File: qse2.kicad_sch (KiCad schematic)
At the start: 81 parts, among them J1 5-1814832-1, J2 5-1814832-1, J3 Conn_02x08_Odd_Even, J4 SJ-3524-SMT, J6 Conn_01x02, J7 B4B-XH-A_LF__SN_, U1 SN74LVC1G14DBV, U10 SN74LVC1G14DBV, U11 NCP114ASN330T1G, U2 SN74LVC1G14DBV, U3 SN74CBT3253, U4 SN74AC74PW, U5 AD8137ARZ-R7, U6 NCV8114ASN165T1G, U7 UA78M05IDCYR, U8 AP2120N-2.5TRG1, U9 AD8137ARZ-R7

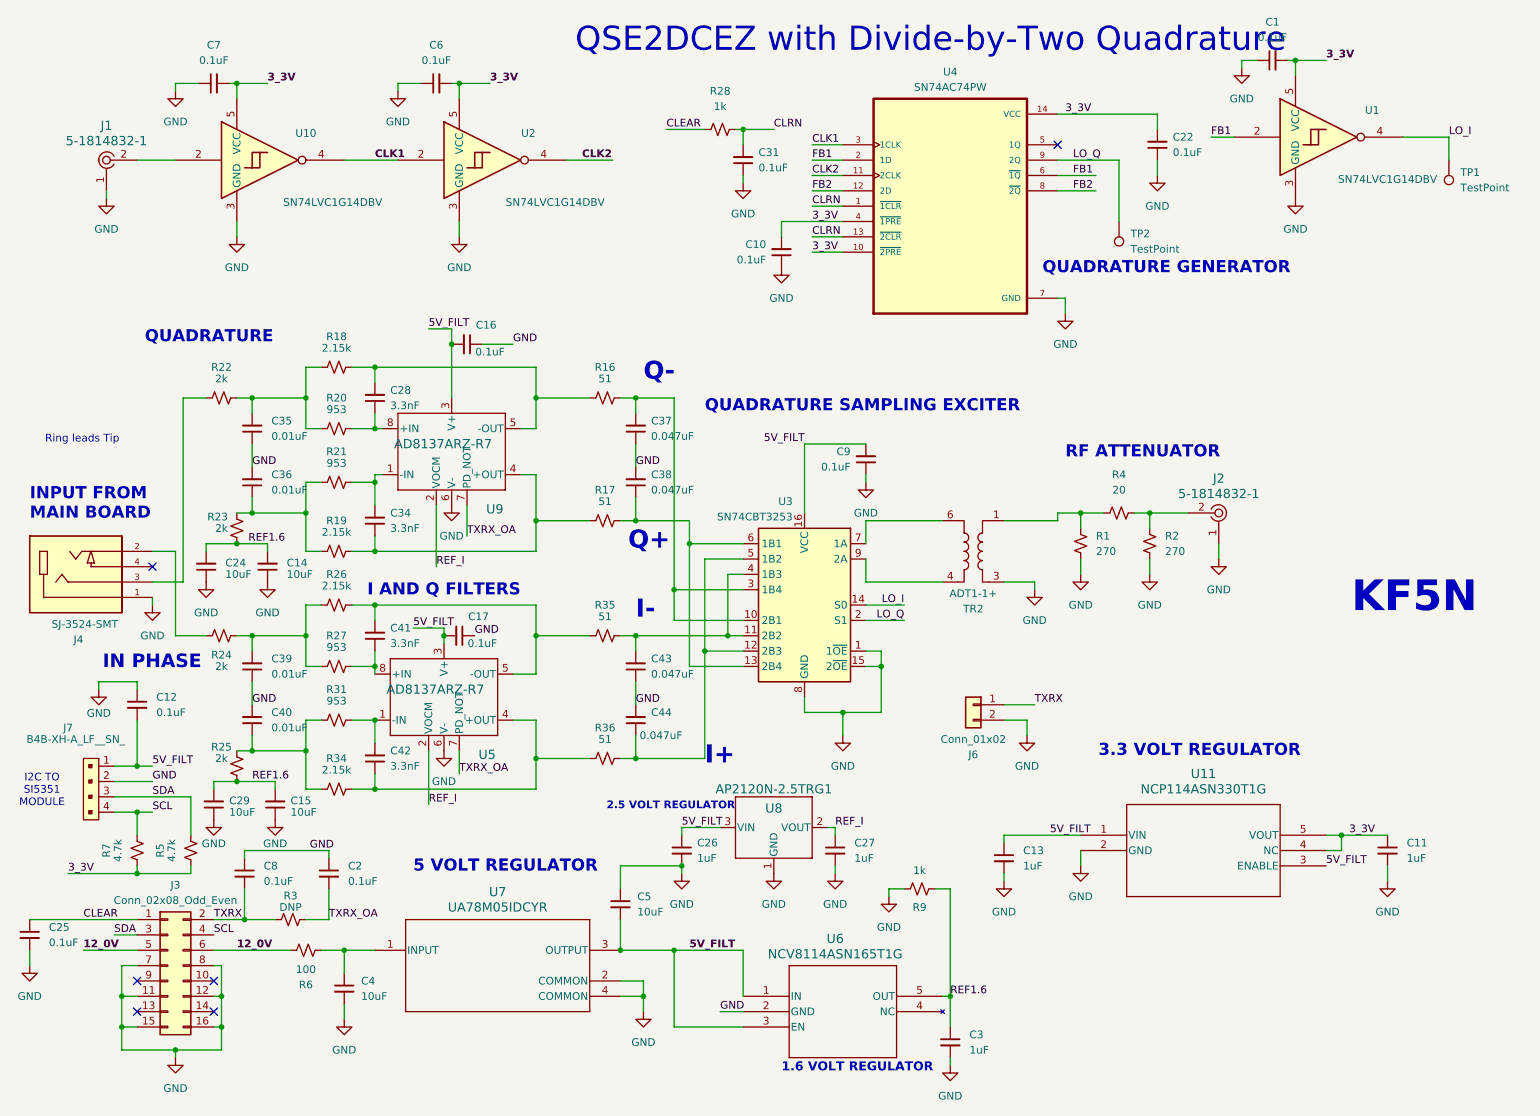
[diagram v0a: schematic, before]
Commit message: Work in progress. Changing reference sources due to supply chain issue.
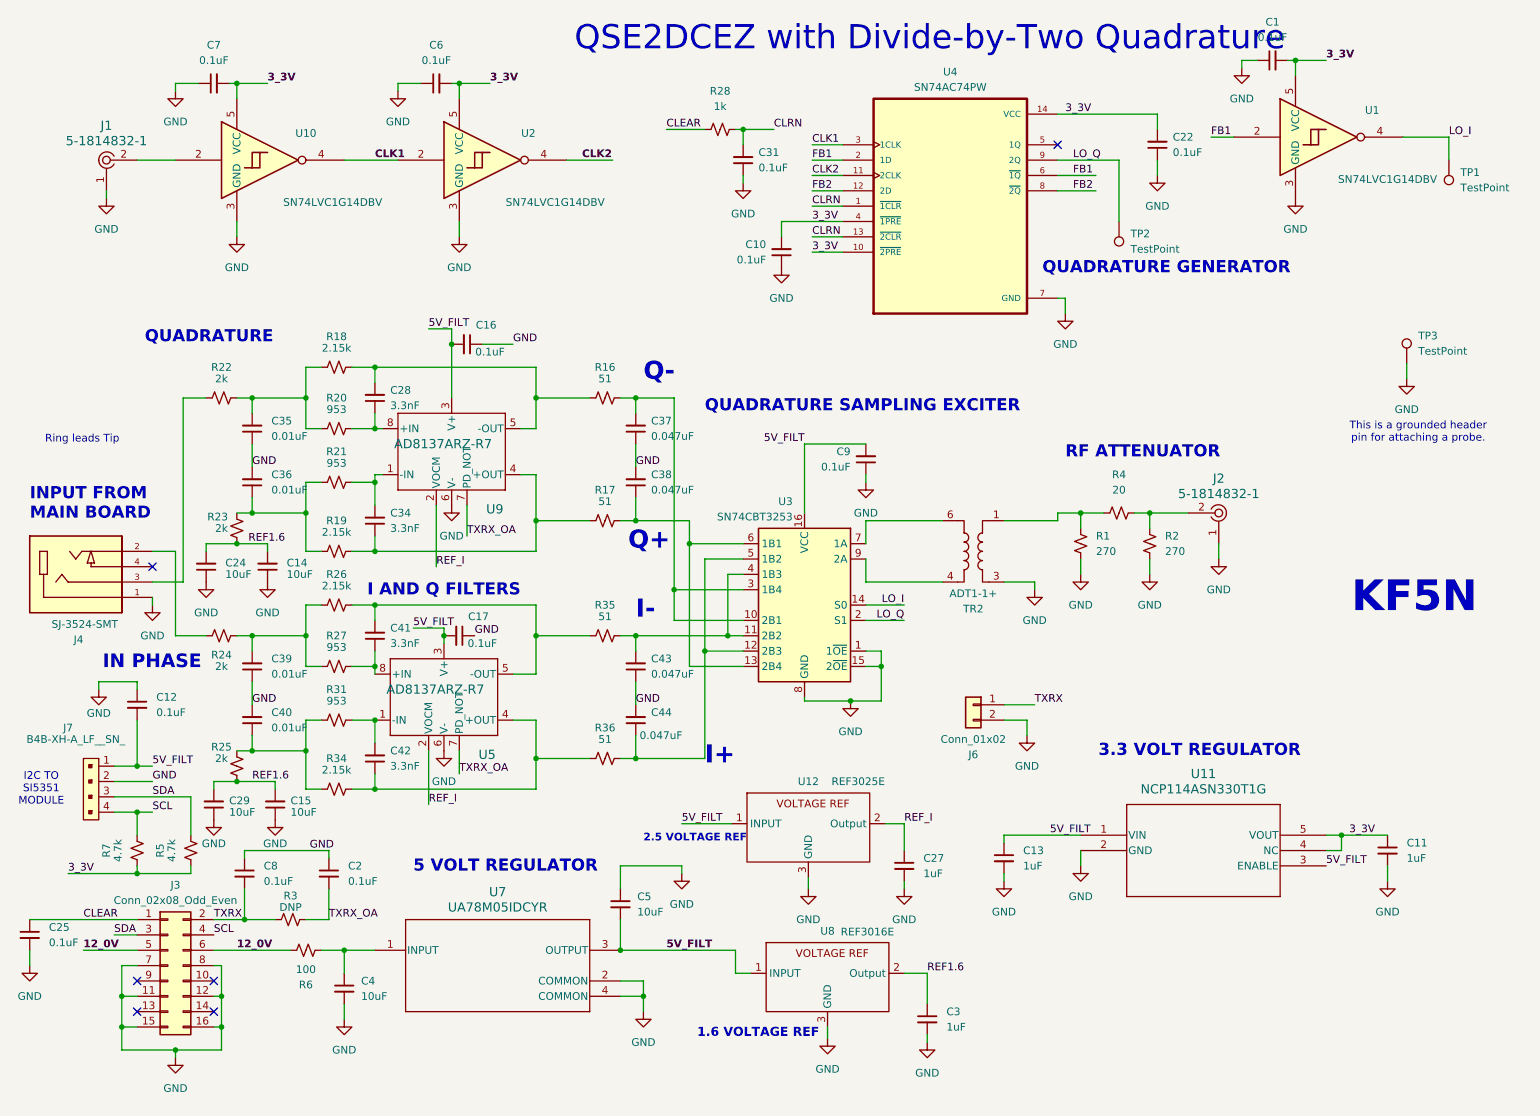
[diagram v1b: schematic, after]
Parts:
- removed C26: 1uF, Capacitor_SMD:C_1206_3216Metric, symbol Device:C_Small
- removed R9: 1k, Resistor_SMD:R_1206_3216Metric, symbol Device:R_Small_US
- removed U6: NCV8114ASN165T1G, TSOP-5-483-N_ONS, symbol NCP115ASN330T2G:NCP115ASN330T2G
- removed U8: AP2120N-2.5TRG1, AP2120N:SOT-23_DIO, symbol 2023-10-04_14-49-55:AP2120N-2.5TRG1
- added TP3: TestPoint, Connector_PinHeader_2.54mm:PinHeader_1x01_P2.54mm_Vertical, symbol Connector:TestPoint
- added U12: REF3025E, Package_TO_SOT_SMD:SOT-23-3, symbol TI_SOT23_vref:TI_SOT-23_vref
- added U8: REF3016E, Package_TO_SOT_SMD:SOT-23-3, symbol TI_SOT23_vref:TI_SOT-23_vref
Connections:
- net 5V_FILT: now also U12.1 (INPUT), U8.1 (INPUT)
- net GND: now also TP3.1, U12.3 (GND), U8.3 (GND)
- net REF1.6: now also U8.2 (Output)
- net REF_I: now also U12.2 (Output)
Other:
- note added: "1.6 VOLTAGE REF"
- note added: "2.5 VOLTAGE REF"
- note added: "This is a grounded header pin for attaching a probe."
- note removed: "1.6 VOLT REGULATOR"
- note removed: "2.5 VOLT REGULATOR"
- moved on the sheet: C27, C3

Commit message: Ready for release to fab.
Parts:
- removed C2: 0.1uF, Capacitor_SMD:C_1206_3216Metric, symbol Device:C_Small
- removed R3: DNP, Resistor_SMD:R_1206_3216Metric, symbol Device:R_Small_US
- removed U12: REF3025E, Package_TO_SOT_SMD:SOT-23-3, symbol TI_SOT23_vref:TI_SOT-23_vref
- added C18: 0.01uF, Capacitor_SMD:C_1206_3216Metric, symbol Device:C_Small
- added C30, C32: 1uF, Capacitor_SMD:C_1206_3216Metric, symbol Device:C_Small
- added R37: 2.2k, Resistor_SMD:R_1206_3216Metric, symbol Device:R_Small_US
- added U6: AP7343, Package_TO_SOT_SMD:TSOT-23-5, symbol AP7343-25W5-7:AP7343
- C27: value 1uF -> 10uF
- C8: value 0.1uF -> 0.01uF
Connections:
- net 5V_FILT: now also C30.1, C32.1, U6.1 (VIN), U6.3 (EN)
- net GND: now also C18.1, C30.2, C32.2, R37.1, U6.2 (GND)
- net REF_I: now also R37.2, U6.5 (VOUT)
- net TXRX: now also C18.2
- net TXRX_OA: no longer names the net of U9.7 (PD_NOT)
- net TXRX_OA: no longer U5.7 (PD_NOT)
- no-connect marks 6 -> 9
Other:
- moved on the sheet: C27

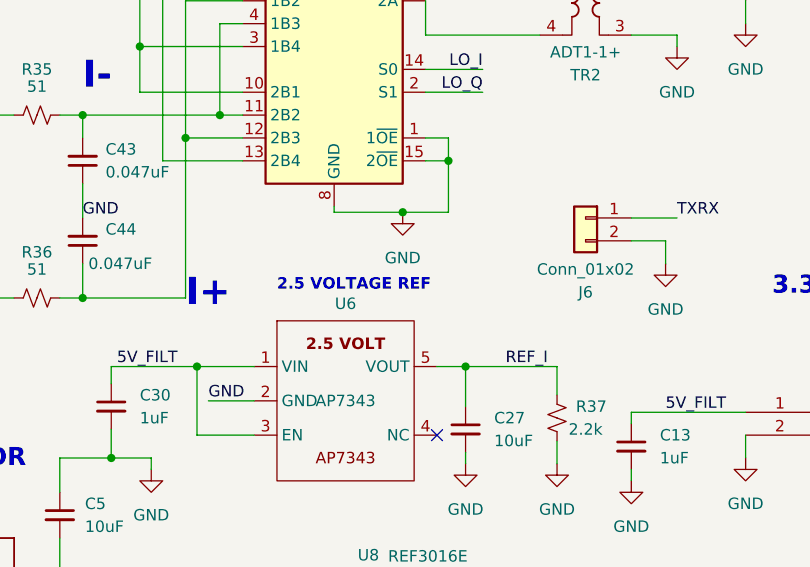
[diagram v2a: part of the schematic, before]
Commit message: Changed text on schematic, very minor change.
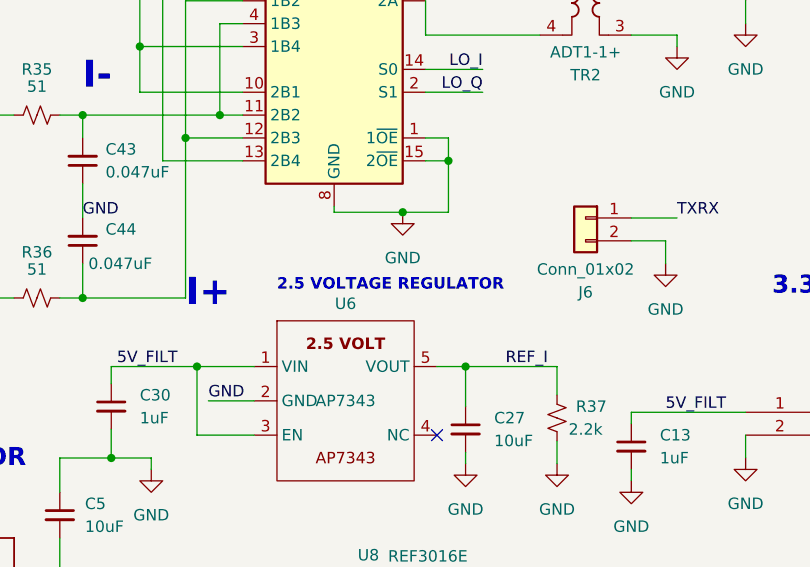
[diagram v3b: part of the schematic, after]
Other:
- note added: "2.5 VOLTAGE REGULATOR"
- note removed: "2.5 VOLTAGE REF"
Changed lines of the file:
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@@
 		)
 	)
-	(text "2.5 VOLTAGE REF"
+	(text "2.5 VOLTAGE REGULATOR"
 		(exclude_from_sim no)
 		(at 138.43 137.795 0)
